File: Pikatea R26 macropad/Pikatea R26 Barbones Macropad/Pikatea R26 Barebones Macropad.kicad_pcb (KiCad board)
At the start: 2 copper layers, 118.3 x 40.8 mm, 20 parts, among them J1 Conn_01x12_Female, SW3 Rotary_Encoder_Switch, U1 ProMicro

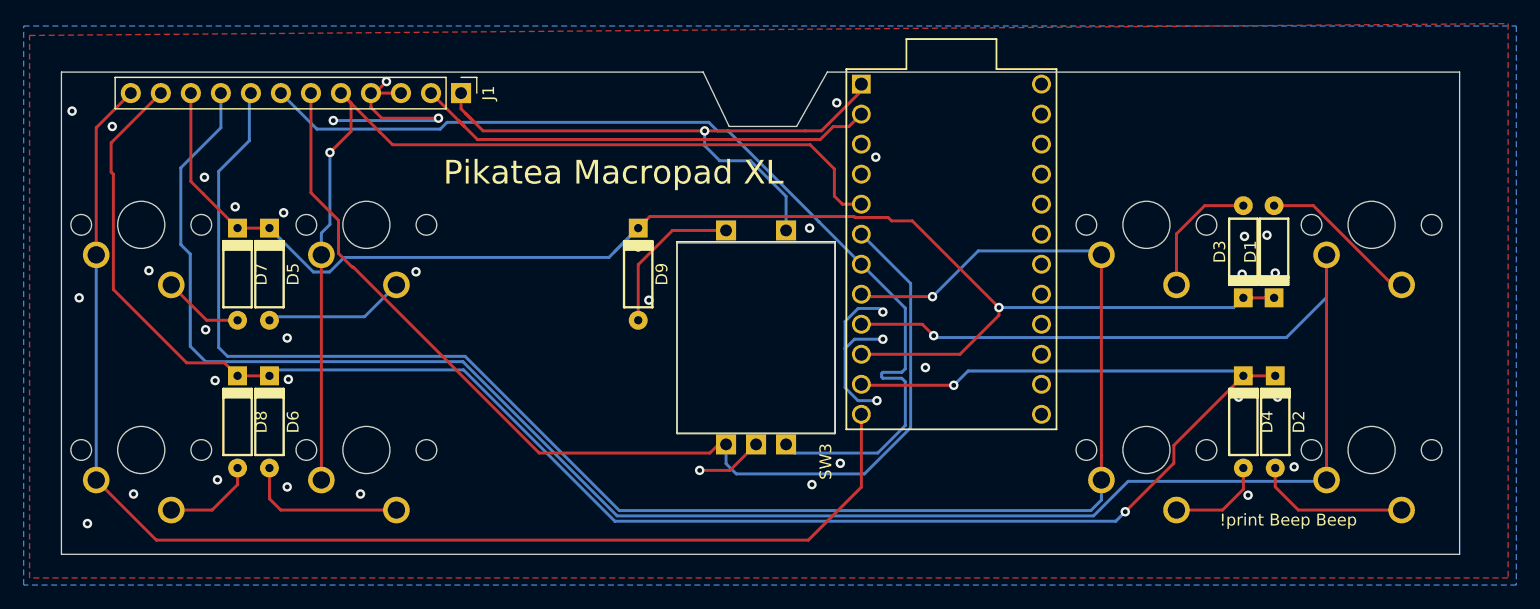
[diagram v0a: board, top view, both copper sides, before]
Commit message: update r26 and gb4
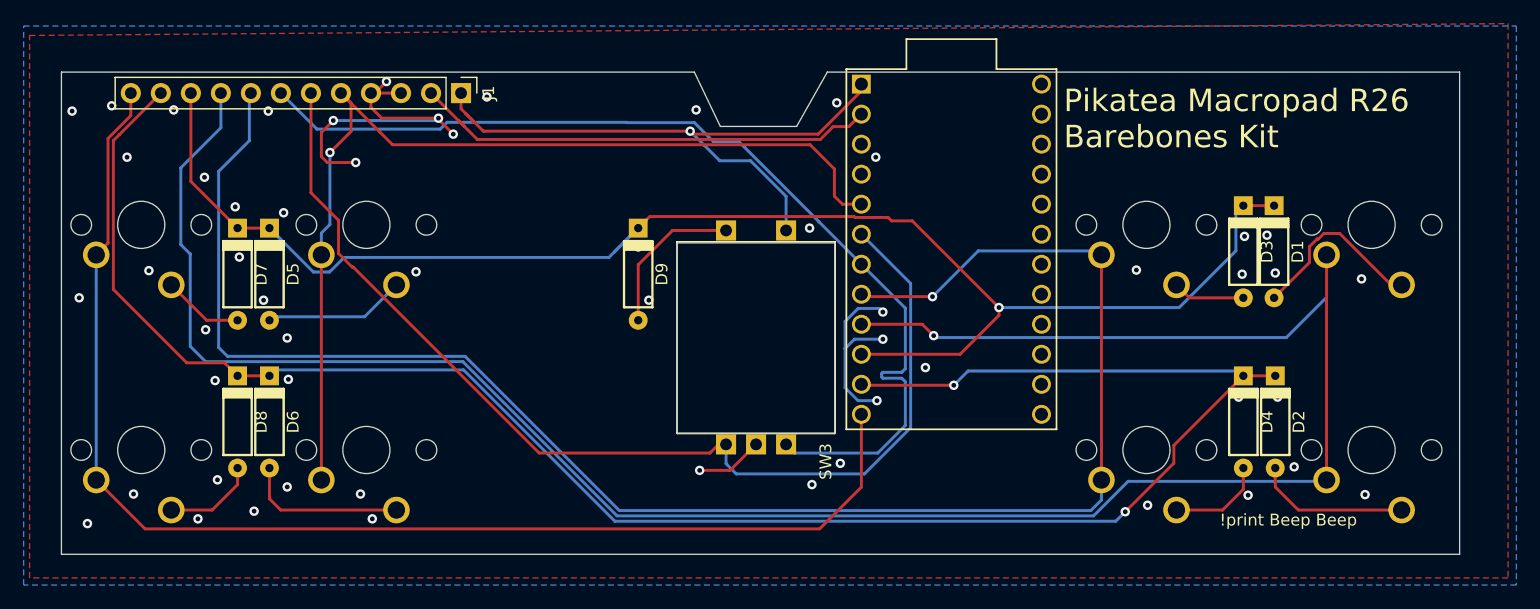
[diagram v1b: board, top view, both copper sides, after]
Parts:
- turned D1 to 270 degrees
- turned D3 to 270 degrees
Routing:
- net GND: track 42.3 -> 50.7 mm, vias 40 -> 56
- net /A3: track 127.3 -> 132.4 mm
- net Net-(D3-Pad2): track 11.0 -> 6.11 mm
- net Net-(D1-Pad2): track 13.6 -> 16.4 mm
- net /A4: track 108.8 -> 108.0 mm
- net /A10: track 51.7 -> 52.4 mm
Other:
- outline, holes or cut-outs redrawn
- board text added: "Pikatea Macropad R26 Barebones Kit"
- board text removed: "Pikatea Macropad XL"
